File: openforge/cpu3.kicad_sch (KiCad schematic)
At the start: 77 parts, among them U5 AM3352BZCZ100

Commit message: added footprint associations
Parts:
- R54: footprint (none) -> Resistor_SMD:R_0402_1005Metric
- TP2, TP3: footprint (none) -> TestPoint:TestPoint_Pad_1.5x1.5mm
- U5: footprint (none) -> footprints:ZCZ0324A
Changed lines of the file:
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@@
 			)
 		)
-		(property "Footprint" ""
+		(property "Footprint" "footprints:ZCZ0324A"
 			(at 278.13 171.45 0)
 			(effects
@@
 			)
 		)
-		(property "Footprint" ""
+		(property "Footprint" "TestPoint:TestPoint_Pad_1.5x1.5mm"
 			(at 217.17 163.83 0)
 			(effects
@@
 			)
 		)
-		(property "Footprint" ""
+		(property "Footprint" "TestPoint:TestPoint_Pad_1.5x1.5mm"
 			(at 328.93 250.19 0)
 			(effects
@@
 			)
 		)
-		(property "Footprint" ""
+		(property "Footprint" "Resistor_SMD:R_0402_1005Metric"
 			(at 342.392 248.92 90)
 			(effects
@@
 			)
 		)
-		(property "Footprint" ""
+		(property "Footprint" "footprints:ZCZ0324A"
 			(at 280.67 313.69 0)
 			(effects

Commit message: PCB all layers copied from beaglebone black
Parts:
- C77: footprint Capacitor_SMD:C_0402_1005Metric -> Capacitor_SMD:C_0805_2012Metric
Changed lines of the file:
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@@
 			)
 		)
-		(property "Footprint" "Capacitor_SMD:C_0402_1005Metric"
+		(property "Footprint" "Capacitor_SMD:C_0805_2012Metric"
 			(at 489.9152 171.45 0)
 			(effects

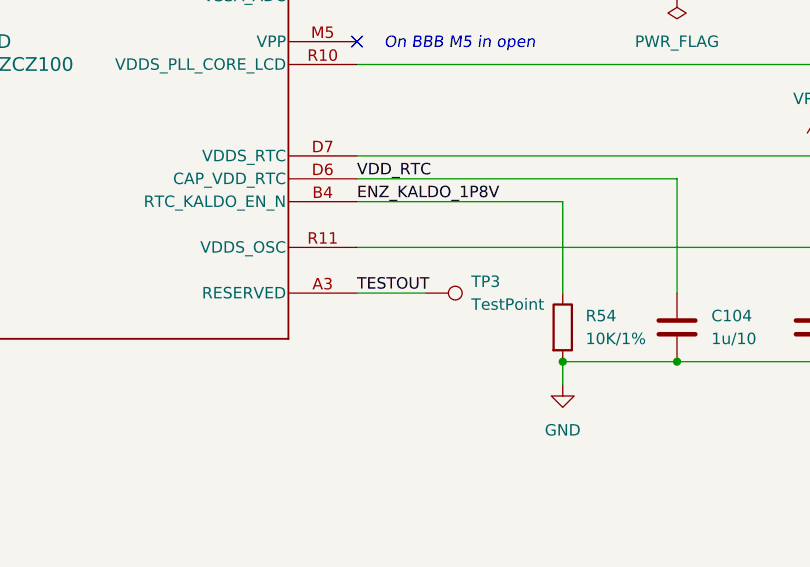
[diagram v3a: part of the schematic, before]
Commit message: fixed various footprints
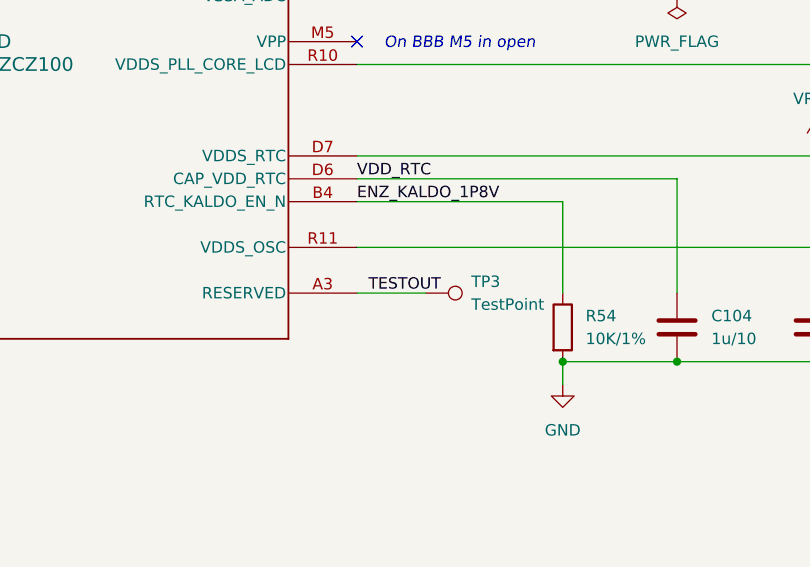
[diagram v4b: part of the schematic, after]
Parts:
- TP2, TP3: footprint TestPoint:TestPoint_Pad_1.5x1.5mm -> TestPoint:TestPoint_Pad_D1.0mm
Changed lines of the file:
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@@
 	)
 	(label "TESTOUT"
-		(at 321.31 245.11 0)
+		(at 322.58 245.11 0)
 		(fields_autoplaced yes)
 		(effects
@@
 			)
 		)
-		(property "Footprint" "TestPoint:TestPoint_Pad_1.5x1.5mm"
+		(property "Footprint" "TestPoint:TestPoint_Pad_D1.0mm"
 			(at 217.17 163.83 0)
 			(effects
@@
 			)
 		)
-		(property "Footprint" "TestPoint:TestPoint_Pad_1.5x1.5mm"
+		(property "Footprint" "TestPoint:TestPoint_Pad_D1.0mm"
 			(at 328.93 250.19 0)
 			(effects

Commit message: fixed all errors and major warnings
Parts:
- C100, C101, C102, C103, C104, C105, C106, C37, C38, C41, C42, C43, C44, C45, C46, C47, C48, C49, C50, C51, C52, C53, C54, C56, C57, C58, C59, C60, C61, C63, C64, C65, C66, C67, C68, C69, C70, C71, C72, C73, C74, C75, C76, C78, C79, C80, C81, C82, C83, C84, C85, C86, C87, C88, C89, C90, C91, C92, C93, C94, C97, C98, C99: footprint Capacitor_SMD:C_0402_1005Metric -> footprints:C_0402_1005Metric
- C39, C40, C55, C62, C77, C95, C96: footprint Capacitor_SMD:C_0805_2012Metric -> footprints:C_0805_2012Metric
- R54: footprint Resistor_SMD:R_0402_1005Metric -> footprints:R_0402_1005Metric
